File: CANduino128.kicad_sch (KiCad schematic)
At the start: 36 parts, among them J1 Conn_01x02, J2 Conn_01x10, U1 AVR-H128-CAN, U2 74AHC373

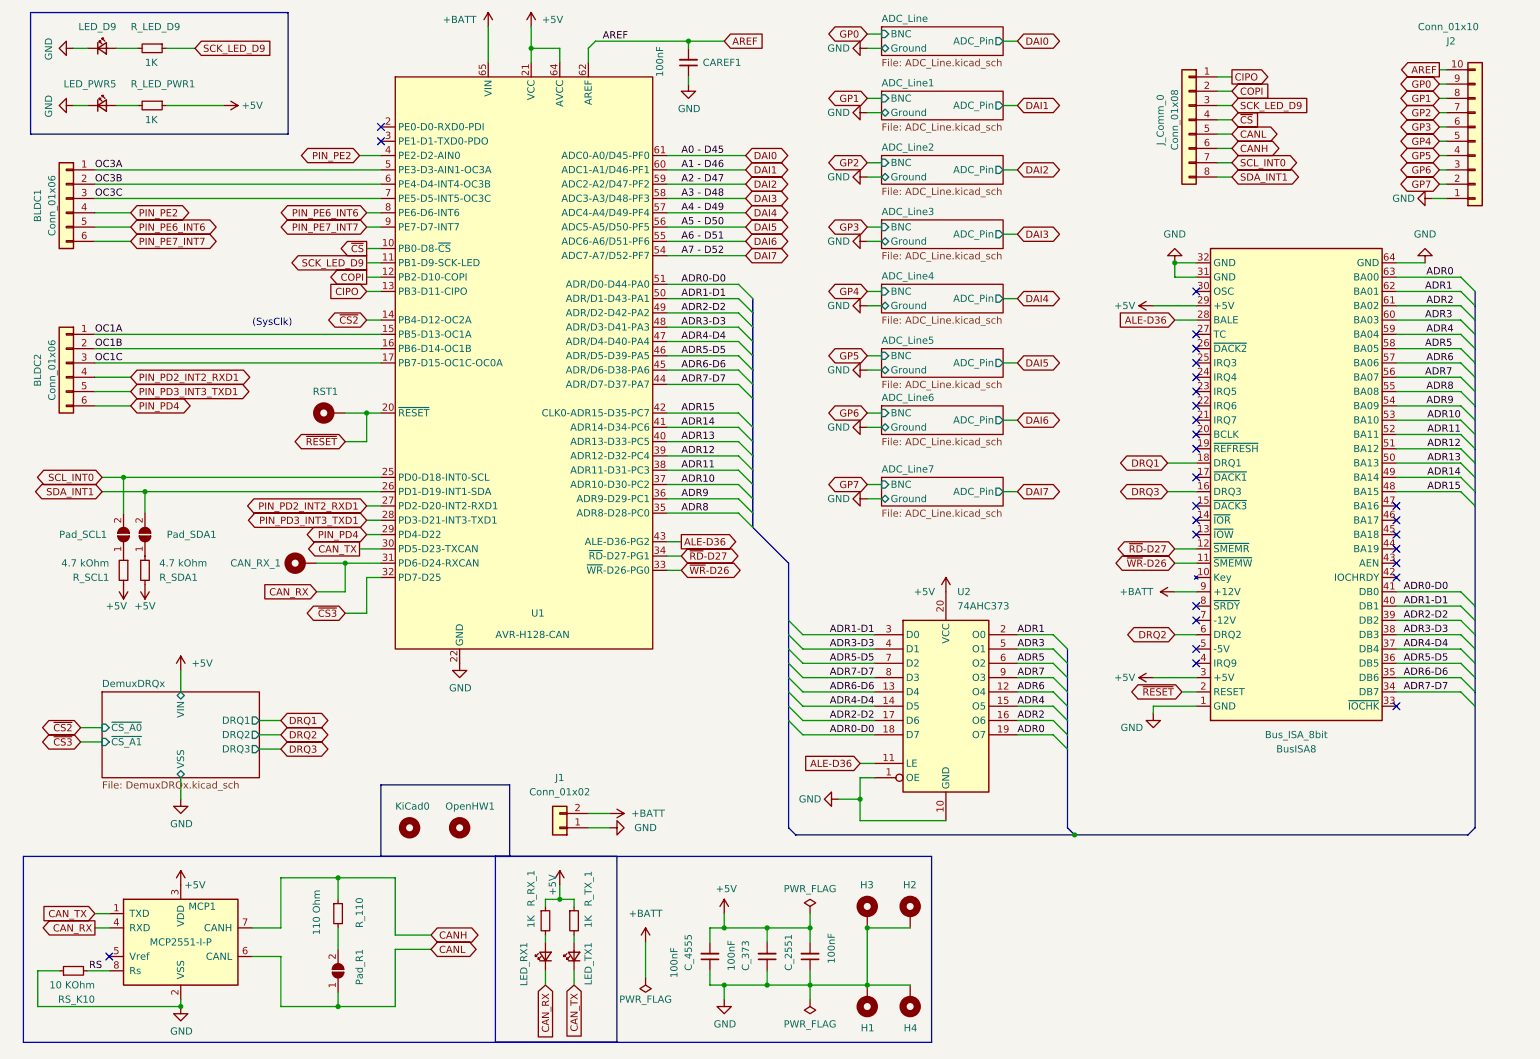
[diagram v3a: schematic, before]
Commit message: Déplacement des connecteurs BLDC Reroute Ajout d'un connecteur ICSP de type USBAsp
git-svn-id: file:///D%5C00%20-%20Dev%20&%20Calculs%5CRepoTortoiseSVN_PCB%5CCANduino128/branches/CANduino128%20-%20v3.x@98 67ddf66f-3787-a644-8df7-7746e21a92b3
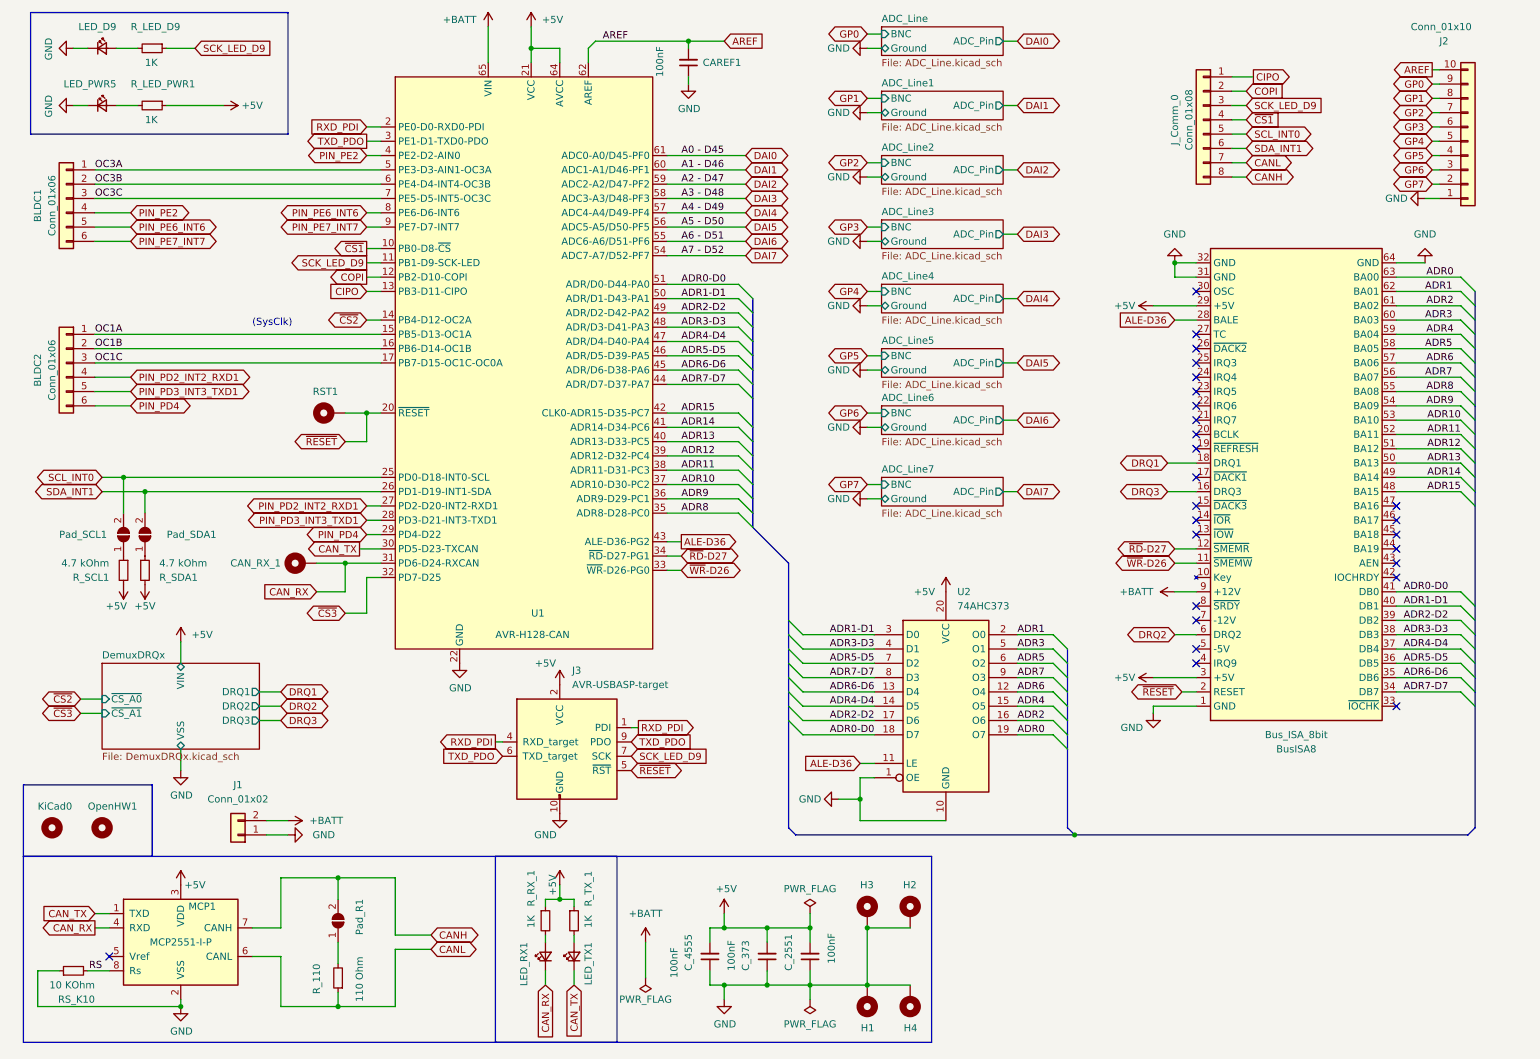
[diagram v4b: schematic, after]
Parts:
- added J3: AVR-USBASP-target, Connector_PinHeader_2.54mm:PinHeader_2x05_P2.54mm_Vertical, symbol AVR_H128-CAN:AVR-USBASP-target
- MCP1: footprint Package_DIP:DIP-8_W7.62mm_Socket_LongPads -> Package_DIP:DIP-8_W7.62mm_Socket
- RST1: footprint TestPoint:TestPoint_Pad_D1.0mm -> Connector_Wire:SolderWire-0.1sqmm_1x01_D0.4mm_OD1mm
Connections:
- net +5V: now also J3.2 (VCC)
- net CANH: now also J_Comm_0.8 (Pin_8), Pad_R1.2 (B); no longer J_Comm_0.6 (Pin_6), R_110.1
- net CANL: now also J_Comm_0.7 (Pin_7), R_110.1; no longer J_Comm_0.5 (Pin_5), Pad_R1.1 (A)
- net GND: now also J3.10 (GND), J3.8 (GND)
- net SCK_LED_D9: now also J3.7 (SCK)
- net SCL_INT0: now also J_Comm_0.5 (Pin_5); no longer J_Comm_0.7 (Pin_7)
- net SDA_INT1: now also J_Comm_0.6 (Pin_6); no longer J_Comm_0.8 (Pin_8)
- net ~{RESET}: now also J3.5 (~{RST})
- net at R_110.2: now also Pad_R1.1 (A); no longer Pad_R1.2 (B)
- net RXD_PDI: now reaches U1.2 (PE0-D0-RXD0-PDI)
- net RXD_PDI: now also J3.1 (PDI), J3.4 (RXD_target)
- net TXD_PDO: now reaches U1.3 (PE1-D1-TXD0-PDO)
- net TXD_PDO: now also J3.6 (TXD_target), J3.9 (PDO)
- net ~{CS} renamed ~{CS1}
- no-connect marks 28 -> 26
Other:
- moved on the sheet: J1, J2, J_Comm_0, KiCad0, OpenHW1, Pad_R1, R_110

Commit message: On se cherche encore sur les /CS qui vont sur les DRQx ou les /DRAQx
git-svn-id: file:///D%5C00%20-%20Dev%20&%20Calculs%5CRepoTortoiseSVN_PCB%5CCANduino128/branches/CANduino128%20-%20v3.x@99 67ddf66f-3787-a644-8df7-7746e21a92b3
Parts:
- J3: footprint Connector_PinHeader_2.54mm:PinHeader_2x05_P2.54mm_Vertical -> Connector_IDC:IDC-Header_2x05_P2.54mm_Vertical
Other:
- sheet DemuxDRQx ports: added ~{DRQ1}, ~{DRQ2}, ~{DRQ3}; removed DRQ1, DRQ2, DRQ3
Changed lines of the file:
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@@
+    )
+  )
+  (global_label "~{DRQ2}" (shape bidirectional) (at 59.69 137.16 0) (fields_autoplaced)
+    (effects (font (size 1.27 1.27)) (justify left))
+    (property "Intersheetrefs" "${INTERSHEET_REFS}" (at 68.8665 137.16 0)
+      (effects (font (size 1.27 1.27)) (justify left) hide)
     )
   )
@@
     )
   )
+  (global_label "~{DRQ3}" (shape bidirectional) (at 59.69 139.7 0) (fields_autoplaced)
+    (effects (font (size 1.27 1.27)) (justify left))
+    (property "Intersheetrefs" "${INTERSHEET_REFS}" (at 68.8665 139.7 0)
+      (effects (font (size 1.27 1.27)) (justify left) hide)
+    )
+  )
   (global_label "DAI0" (shape bidirectional) (at 142.24 39.37 0) (fields_autoplaced)
     (effects (font (size 1.27 1.27)) (justify left))
@@
     )
   )
-  (global_label "DRQ2" (shape bidirectional) (at 59.69 137.16 0) (fields_autoplaced)
-    (effects (font (size 1.27 1.27)) (justify left))
-    (property "Intersheetrefs" "${INTERSHEET_REFS}" (at 68.8665 137.16 0)
-      (effects (font (size 1.27 1.27)) (justify left) hide)
-    )
-  )
   (global_label "~{RD}-D27" (shape bidirectional) (at 130.81 110.49 0) (fields_autoplaced)
     (effects (font (size 1.27 1.27)) (justify left))
@@
     )
   )
-  (global_label "DRQ1" (shape bidirectional) (at 59.69 134.62 0) (fields_autoplaced)
+  (global_label "~{DRQ1}" (shape bidirectional) (at 59.69 134.62 0) (fields_autoplaced)
     (effects (font (size 1.27 1.27)) (justify left))
     (property "Intersheetrefs" "${INTERSHEET_REFS}" (at 68.8665 134.62 0)
@@
     (property "Intersheetrefs" "${INTERSHEET_REFS}" (at 53.8902 104.0606 0)
       (effects (font (size 1.27 1.27)) (justify right) hide)
-    )
-  )
-  (global_label "DRQ3" (shape bidirectional) (at 59.69 139.7 0) (fields_autoplaced)
-    (effects (font (size 1.27 1.27)) (justify left))
-    (property "Intersheetrefs" "${INTERSHEET_REFS}" (at 68.8665 139.7 0)
-      (effects (font (size 1.27 1.27)) (justify left) hide)
     )
   )
@@
       (effects (font (size 1.27 1.27)) (justify left))
     )
-    (property "Footprint" "Connector_PinHeader_2.54mm:PinHeader_2x05_P2.54mm_Vertical" (at 105.41 144.78 90)
+    (property "Footprint" "Connector_IDC:IDC-Header_2x05_P2.54mm_Vertical" (at 105.41 144.78 90)
       (effects (font (size 1.27 1.27)) hide)
     )
@@
       (effects (font (size 1.27 1.27)) (justify left))
     )
-    (pin "DRQ3" output (at 55.88 139.7 0)
+    (pin "~{CS_A0}" input (at 27.94 135.89 180)
+      (effects (font (size 1.27 1.27)) (justify left))
+    )
+    (pin "~{CS_A1}" input (at 27.94 138.43 180)
+      (effects (font (size 1.27 1.27)) (justify left))
+    )
+    (pin "~{DRQ2}" output (at 55.88 137.16 0)
       (effects (font (size 1.27 1.27)) (justify right))
     )
-    (pin "DRQ2" output (at 55.88 137.16 0)
+    (pin "~{DRQ3}" output (at 55.88 139.7 0)
       (effects (font (size 1.27 1.27)) (justify right))
     )
-    (pin "DRQ1" output (at 55.88 134.62 0)
+    (pin "~{DRQ1}" output (at 55.88 134.62 0)
       (effects (font (size 1.27 1.27)) (justify right))
     )
-    (pin "~{CS_A0}" input (at 27.94 135.89 180)
-      (effects (font (size 1.27 1.27)) (justify left))
-    )
-    (pin "~{CS_A1}" input (at 27.94 138.43 180)
-      (effects (font (size 1.27 1.27)) (justify left))
-    )
-    (instances
+    (instances

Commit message: Last version pour la v3.2 On arrête les frais sur cette carte
git-svn-id: file:///D%5C00%20-%20Dev%20&%20Calculs%5CRepoTortoiseSVN_PCB%5CCANduino128/branches/CANduino128%20-%20v3.x@100 67ddf66f-3787-a644-8df7-7746e21a92b3
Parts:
- removed C_4555: 100nF, Capacitor_SMD:C_1210_3225Metric_Pad1.33x2.70mm_HandSolder, symbol Device:C_Small
- removed RST1: MountingHole_Pad, Connector_Wire:SolderWire-0.1sqmm_1x01_D0.4mm_OD1mm, symbol Mechanical:MountingHole_Pad
- Pad_SCL1, Pad_SDA1: footprint Jumper:SolderJumper-2_P1.3mm_Open_TrianglePad1.0x1.5mm -> Connector_PinHeader_2.54mm:PinHeader_1x02_P2.54mm_Vertical
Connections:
- net ~{CS2} is gone; now on net SysClk: U1.14 (PB4-D12-OC2A)
- net ADR15: now also BusISA8.30 (OSC)
- net CANH: now also J_Comm_0.6 (Pin_6); no longer J_Comm_0.8 (Pin_8)
- net CANL: now also J_Comm_0.5 (Pin_5); no longer J_Comm_0.7 (Pin_7)
- net RXD_PDI: no longer J3.4 (RXD_target)
- net SCL_INT0: now also J_Comm_0.7 (Pin_7); no longer J_Comm_0.5 (Pin_5)
- net SDA_INT1: now also J_Comm_0.8 (Pin_8); no longer J_Comm_0.6 (Pin_6)
- net TXD_PDO: no longer J3.6 (TXD_target)
- net ~{CS3}: now also BusISA8.44 (BA19)
- net SysClk: now reaches BusISA8.20 (BCLK)
- net DRQ1: no longer names the net of BusISA8.18 (DRQ1)
- net DRQ2: no longer names the net of BusISA8.6 (DRQ2)
- net DRQ3: no longer names the net of BusISA8.16 (DRQ3)
- no-connect marks 26 -> 28
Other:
- removed sheet DemuxDRQx
- moved on the sheet: J1, J3
